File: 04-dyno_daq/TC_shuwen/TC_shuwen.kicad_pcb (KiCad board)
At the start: 2 copper layers, 36.2 x 20.6 mm, 11 parts, among them J1 Conn_01x04, J2 Conn_01x02, U1 INA333xxDGK

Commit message: added gerber files
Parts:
- moved C1 1.23 mm to (136.6, 77.4)
- moved J2 1.23 mm to (122.6, 79.6)
- moved J1 1.23 mm to (143.3, 79.1)
- moved R1 1.23 mm to (129.8, 80.8)
- moved R2 1.23 mm to (129.8, 82.3)
- moved R3 1.23 mm to (135.8, 80.6)
- moved R4 1.23 mm to (136.3, 81.8)
- moved RG1 1.23 mm to (132.7, 75.3)
- moved U1 1.23 mm to (132.7, 77.9)

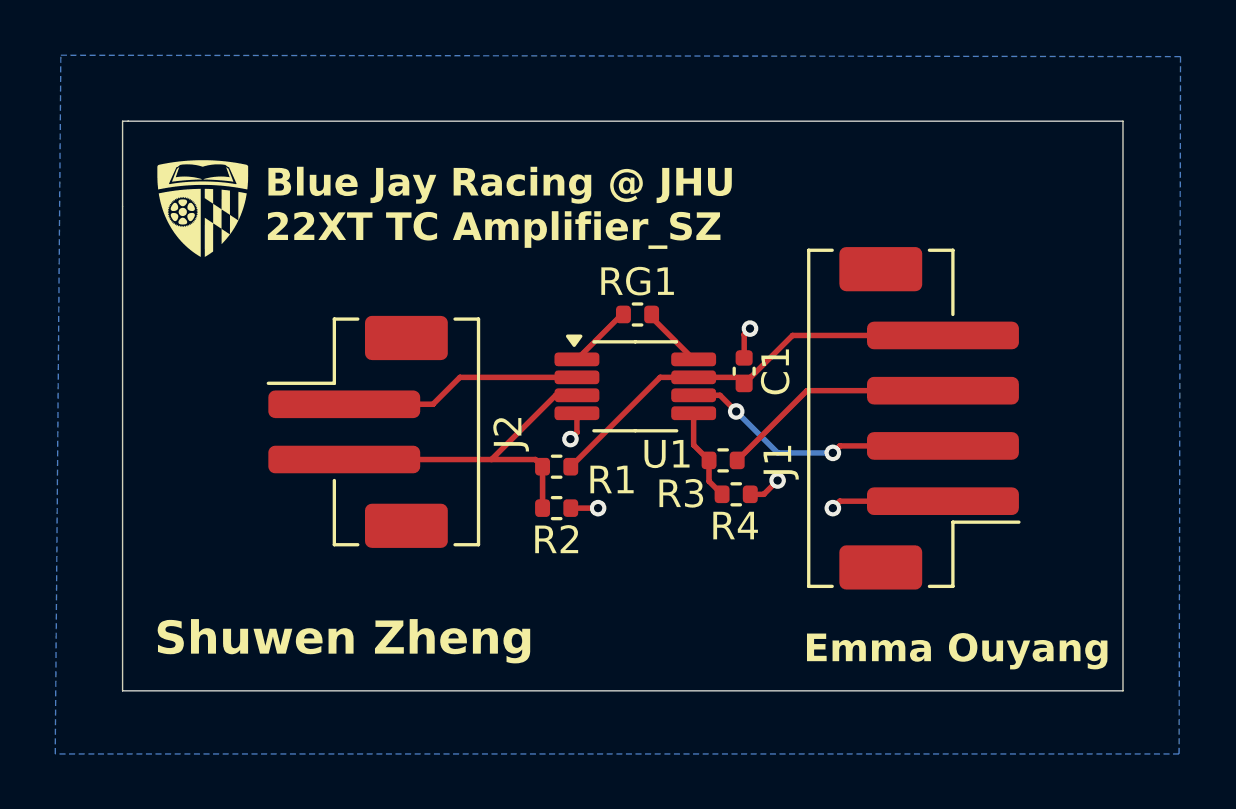
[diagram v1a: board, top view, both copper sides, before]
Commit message: changed jst connector
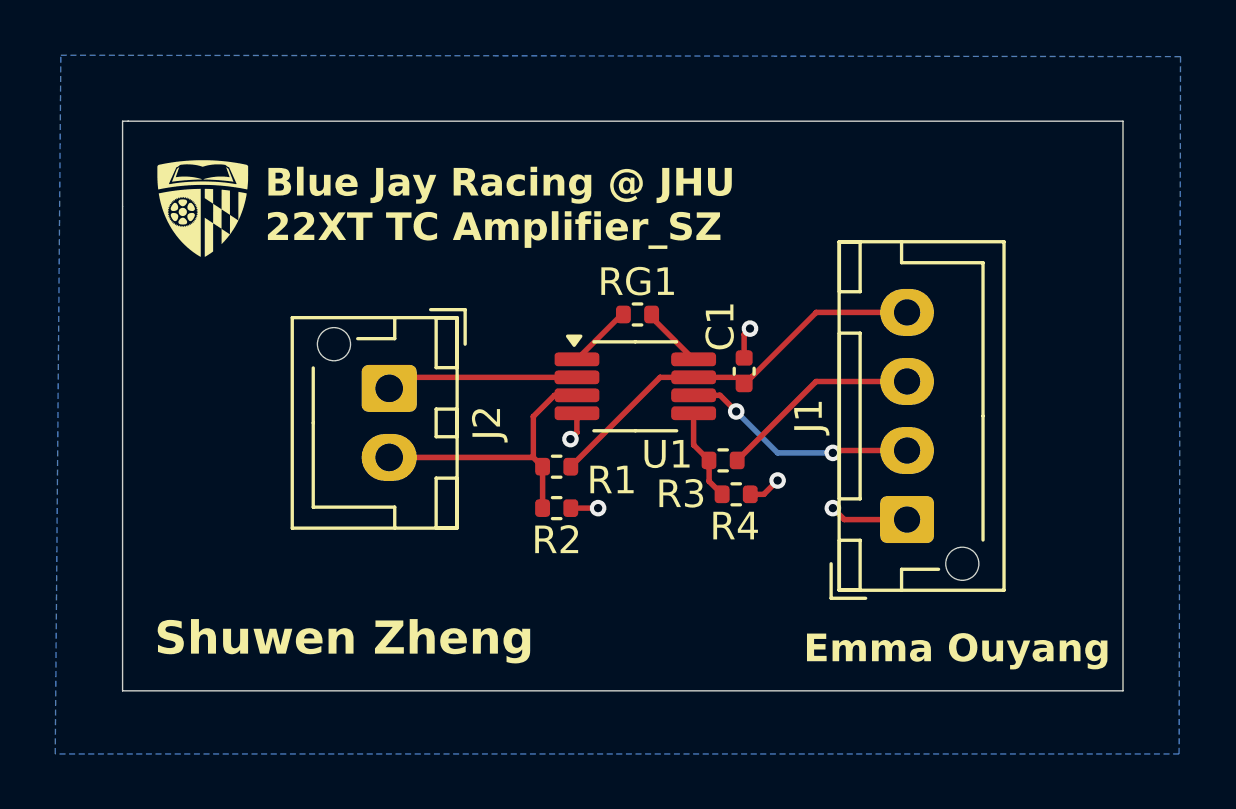
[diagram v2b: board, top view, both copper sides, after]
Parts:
- J1: footprint Connector_JST:JST_PH_B4B-PH-SM4-TB_1x04-1MP_P2.00mm_Vertical -> Connector_JST:JST_XH_B4B-XH-AM_1x04_P2.50mm_Vertical
- J2: footprint Connector_JST:JST_PH_B2B-PH-SM4-TB_1x02-1MP_P2.00mm_Vertical -> Connector_JST:JST_XH_B2B-XH-AM_1x02_P2.50mm_Vertical
- moved J1 3.75 mm to (142.5, 82.8)
- moved J2 1.94 mm to (123.8, 78.0)
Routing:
- net TC+: track 12.8 -> 10.6 mm
- net TC-: track 8.83 -> 6.96 mm
- net TC_AMP_OUT: track 9.99 -> 8.63 mm
- net GND: track 8.46 -> 7.23 mm
- net 5v_ref: track 8.50 -> 7.33 mm
- net 5v_buck: track 15.4 -> 14.8 mm

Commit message: modified tc shuwen dimensions
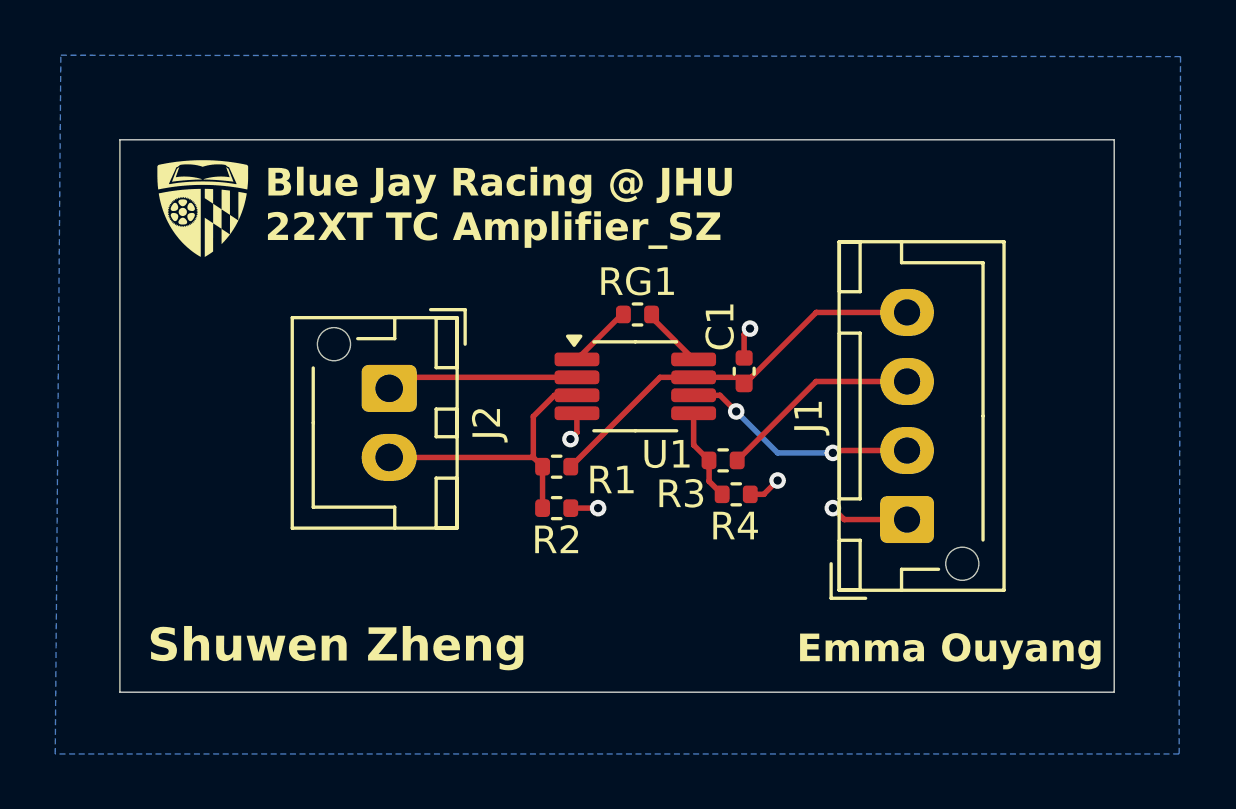
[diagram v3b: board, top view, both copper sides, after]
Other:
- board size 36.2 x 20.6 mm -> 36 x 20 mm
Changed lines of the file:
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@@
 			(usegerberattributes no)
 			(usegerberadvancedattributes no)
-			(creategerberjobfile yes)
+			(creategerberjobfile no)
 			(dashed_line_dash_ratio 12.000000)
 			(dashed_line_gap_ratio 3.000000)
@@
 	)
 	(gr_line
-		(start 114.0968 71.4248)
-		(end 114.0968 68.326)
+		(start 114 89)
+		(end 114 69)
 		(stroke
 			(width 0.05)
-			(type default)
+			(type solid)
 		)
 		(layer "Edge.Cuts")
 	)
 	(gr_line
-		(start 114.3 68.326)
-		(end 150.3172 68.326)
+		(start 150 89)
+		(end 150 69)
 		(stroke
 			(width 0.05)
-			(type default)
+			(type solid)
 		)
 		(layer "Edge.Cuts")
 	)
 	(gr_line
-		(start 150.3172 68.326)
-		(end 150.3172 88.9508)
+		(start 150 69)
+		(end 114 69)
 		(stroke
 			(width 0.05)
-			(type default)
+			(type solid)
 		)
 		(layer "Edge.Cuts")
 	)
 	(gr_line
-		(start 114.0968 88.9508)
-		(end 114.0968 71.4248)
+		(start 150 89)
+		(end 114 89)
 		(stroke
 			(width 0.05)
-			(type default)
-		)
-		(layer "Edge.Cuts")
-	)
-	(gr_line
-		(start 114.0968 68.326)
-		(end 114.3 68.326)
-		(stroke
-			(width 0.05)
-			(type default)
-		)
-		(layer "Edge.Cuts")
-	)
-	(gr_line
-		(start 150.3172 88.9508)
-		(end 114.0968 88.9508)
-		(stroke
-			(width 0.05)
-			(type default)
+			(type solid)
 		)
 		(layer "Edge.Cuts")
 	)
 	(gr_text "Emma Ouyang\n"
-		(at 138.75 88 -0)
+		(at 138.5 88 -0)
 		(layer "F.SilkS")
 		(effects
@@
 	)
 	(gr_text "Shuwen Zheng"
-		(at 115.25 87.75 -0)
+		(at 115 88 -0)
 		(layer "F.SilkS")
 		(effects
@@
 	)
 	(gr_text "Blue Jay Racing @ JHU\n22XT\nTC Amplifier_SZ"
-		(at 143.75 74.5 -0)
+		(at 139.5 74.5 -0)
 		(layer "B.SilkS")
 		(effects
@@
 		)
 	)
+	(dimension
+		(type orthogonal)
+		(layer "Dwgs.User")
+		(pts
+			(xy 114 89) (xy 114 69)
+		)
+		(height -3.75)
+		(orientation 1)
+		(format
+			(prefix "")
+			(suffix "")
+			(units 3)
+			(units_format 0)
+			(precision 4)
+			(suppress_zeroes yes)
+		)
+		(style
+			(thickness 0.2)
+			(arrow_length 1.27)
+			(text_position_mode 0)
+			(arrow_direction outward)
+			(extension_height 0.58642)
+			(extension_offset 0.5)
+			(keep_text_aligned yes)
+		)
+		(gr_text "20"
+			(at 108.45 79 90)
+			(layer "Dwgs.User")
+			(effects
+				(font
+					(size 1.5 1.5)
+					(thickness 0.3)
+				)
+			)
+		)
+	)
+	(dimension
+		(type orthogonal)
+		(layer "Dwgs.User")
+		(pts
+			(xy 114 89) (xy 150 89)
+		)
+		(height 5)
+		(orientation 0)
+		(format
+			(prefix "")
+			(suffix "")
+			(units 3)
+			(units_format 0)
+			(precision 4)
+			(suppress_zeroes yes)
+		)
+		(style
+			(thickness 0.2)
+			(arrow_length 1.27)
+			(text_position_mode 0)
+			(arrow_direction outward)
+			(extension_height 0.58642)
+			(extension_offset 0.5)
+			(keep_text_aligned yes)
+		)
+		(gr_text "36"
+			(at 132 92.2 0)
+			(layer "Dwgs.User")
+			(effects
+				(font
+					(size 1.5 1.5)
+					(thickness 0.3)
+				)
+			)
+		)
+	)

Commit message: Updated grounding for temp pcbs
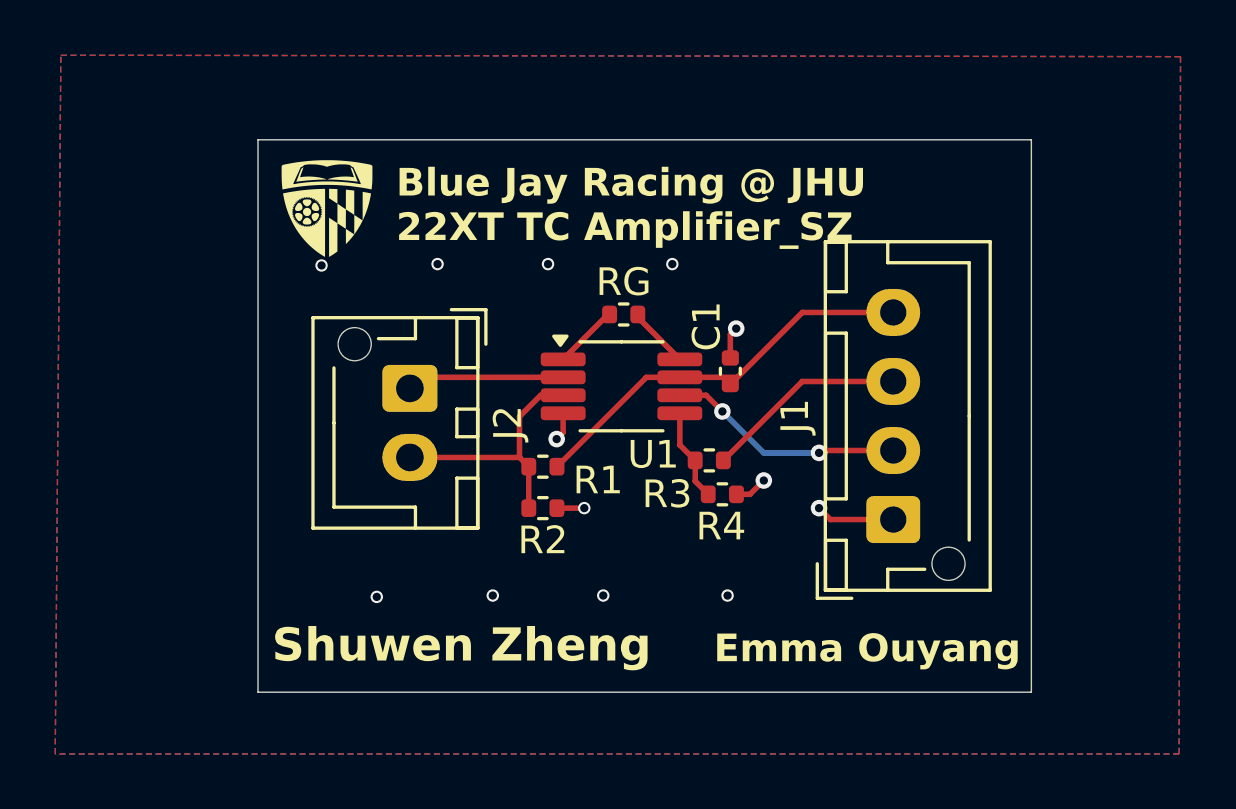
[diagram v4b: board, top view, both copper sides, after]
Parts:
- moved G*** 4.50 mm to (121.5, 71.5)
- moved G*** 2.37 mm to (144.5, 71.5)
- moved J2 0.75 mm to (124.5, 78.0)
- moved C1 0.50 mm to (136.1, 77.4)
- moved J1 0.50 mm to (142.0, 82.8)
- moved R1 0.50 mm to (129.3, 80.8)
- moved R2 0.50 mm to (129.3, 82.3)
- moved R3 0.50 mm to (135.3, 80.6)
- moved R4 0.50 mm to (135.8, 81.8)
- moved RG 0.50 mm to (132.2, 75.3)
- moved U1 0.50 mm to (132.2, 77.9)
- renumbered RG1 to RG
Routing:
- net TC-: track 6.96 -> 5.71 mm
- net TC+: track 10.6 -> 9.32 mm
- net GND: vias 5 -> 13
- added copper zone on F.Cu, net GND
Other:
- board size 36 x 20 mm -> 28 x 20 mm

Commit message: Added silkscreen descriptor text + kent's name to TC shuwen
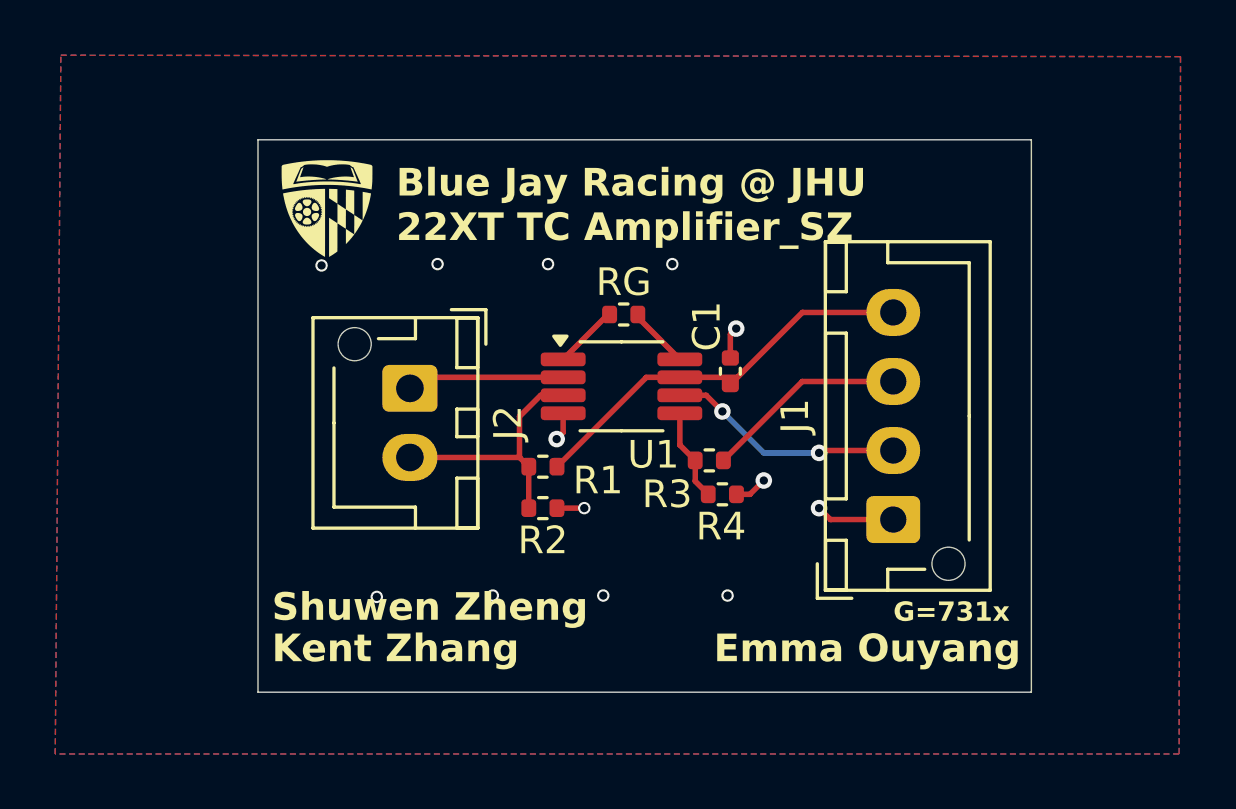
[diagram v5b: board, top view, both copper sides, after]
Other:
- board text added: "5v_buck"
- board text added: "5v_ref"
- board text added: "G=731x"
- board text added: "GND"
- board text added: "Kent Zhang"
- board text added: "TC+"
- board text added: "TC-"
- board text added: "TC_amp_out"
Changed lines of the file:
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@@
+		)
+	)
+	(gr_text "Kent Zhang"
+		(at 119.5 88 0)
+		(layer "F.SilkS")
+		(effects
+			(font
+				(size 1 1)
+				(thickness 0.2)
+				(bold yes)
+			)
+			(justify left bottom)
+		)
+	)
+	(gr_text "G=731x"
+		(at 142 86.5 0)
+		(layer "F.SilkS")
+		(effects
+			(font
+				(size 0.7 0.7)
+				(thickness 0.14)
+				(bold yes)
+			)
+			(justify left bottom)
 		)
 	)
@@
 	)
 	(gr_text "Shuwen Zheng"
-		(at 119.5 88 -0)
+		(at 119.5 86.5 0)
 		(layer "F.SilkS")
 		(effects
 			(font
-				(size 1.2 1.2)
-				(thickness 0.25)
+				(size 1 1)
+				(thickness 0.2)
 				(bold yes)
 			)
@@
 	)
 	(gr_text "Shuwen Zheng"
-		(at 133 85.25 0)
-		(layer "B.SilkS")
-		(effects
-			(font
-				(size 1.2 1.2)
-				(thickness 0.25)
-				(bold yes)
-			)
-			(justify left bottom mirror)
-		)
-	)
-	(gr_text "Emma Ouyang\n"
-		(at 130.5 87 0)
+		(at 130.5 86 -0)
 		(layer "B.SilkS")
 		(effects
@@
 		)
 	)
-	(gr_text "Blue Jay Racing @ JHU\n22XT\nTC Amplifier_SZ"
-		(at 141.5 74.5 -0)
+	(gr_text "Emma Ouyang\n"
+		(at 146 87.5 0)
 		(layer "B.SilkS")
 		(effects
+			(font
+				(size 1 1)
+				(thickness 0.2)
+				(bold yes)
+			)
+			(justify left bottom mirror)
+		)
+	)
+	(gr_text "GND"
+		(at 140 83 0)
+		(layer "B.SilkS")
+		(effects
+			(font
+				(size 0.8 0.8)
+				(thickness 0.16)
+				(bold yes)
+			)
+			(justify left bottom mirror)
+		)
+	)
+	(gr_text "5v_ref"
+		(at 140.5 78 0)
+		(layer "B.SilkS")
+		(effects
+			(font
+				(size 0.8 0.8)
+				(thickness 0.16)
+				(bold yes)
+			)
+			(justify left bottom mirror)
+		)
+	)
+	(gr_text "5v_buck"
+		(at 140.5 76 0)
+		(layer "B.SilkS")
+		(effects
+			(font
+				(size 0.8 0.8)
+				(thickness 0.16)
+				(bold yes)
+			)
+			(justify left bottom mirror)
+		)
+	)
+	(gr_text "TC_amp_out"
+		(at 140.5 80.5 0)
+		(layer "B.SilkS")
+		(effects
+			(font
+				(size 0.8 0.8)
+				(thickness 0.16)
+				(bold yes)
+			)
+			(justify left bottom mirror)
+		)
+	)
+	(gr_text "G=731x"
+		(at 143 86 -0)
+		(layer "B.SilkS")
+		(effects
+			(font
+				(size 0.7 0.7)
+				(thickness 0.14)
+				(bold yes)
+			)
+			(justify left bottom mirror)
+		)
+	)
+	(gr_text "TC+"
+		(at 129 81 0)
+		(layer "B.SilkS")
+		(effects
+			(font
+				(size 0.8 0.8)
+				(thickness 0.16)
+				(bold yes)
+			)
+			(justify left bottom mirror)
+		)
+	)
+	(gr_text "Kent Zhang"
+		(at 130.5 87.5 -0)
+		(layer "B.SilkS")
+		(effects
+			(font
+				(size 1 1)
+				(thickness 0.2)
+				(bold yes)
+			)
+			(justify left bottom mirror)
+		)
+	)
+	(gr_text "TC-"
+		(at 129 78.5 0)
+		(layer "B.SilkS")
+		(effects
+			(font
+				(size 0.8 0.8)
+				(thickness 0.16)
+				(bold yes)
+			)
+			(justify left bottom mirror)
+		)
+	)
+	(gr_text "Blue Jay Racing @ JHU\n22XT\nTC Amplifier_SZ"
+		(at 141 74.5 -0)
+		(layer "B.SilkS")
+		(effects
